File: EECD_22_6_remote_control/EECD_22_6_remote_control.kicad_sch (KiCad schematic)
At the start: 22 parts

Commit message: Add files via upload
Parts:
- gave numbers to parts that had none: 13
- renumbered C to C1
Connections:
- no-connect marks 5 -> 124

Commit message: you can understand at least smth now
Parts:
- C1: value 100u -> 10u
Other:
- note added: "BATTERY"
- note added: "JOYSTICK"
- note added: "LEDs"
- note added: "NRF24"
- moved on the sheet: BT1, BT2, BT3, C1, D1, D2, D3, DC/DC_bck1, R1, R2, R3, R4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

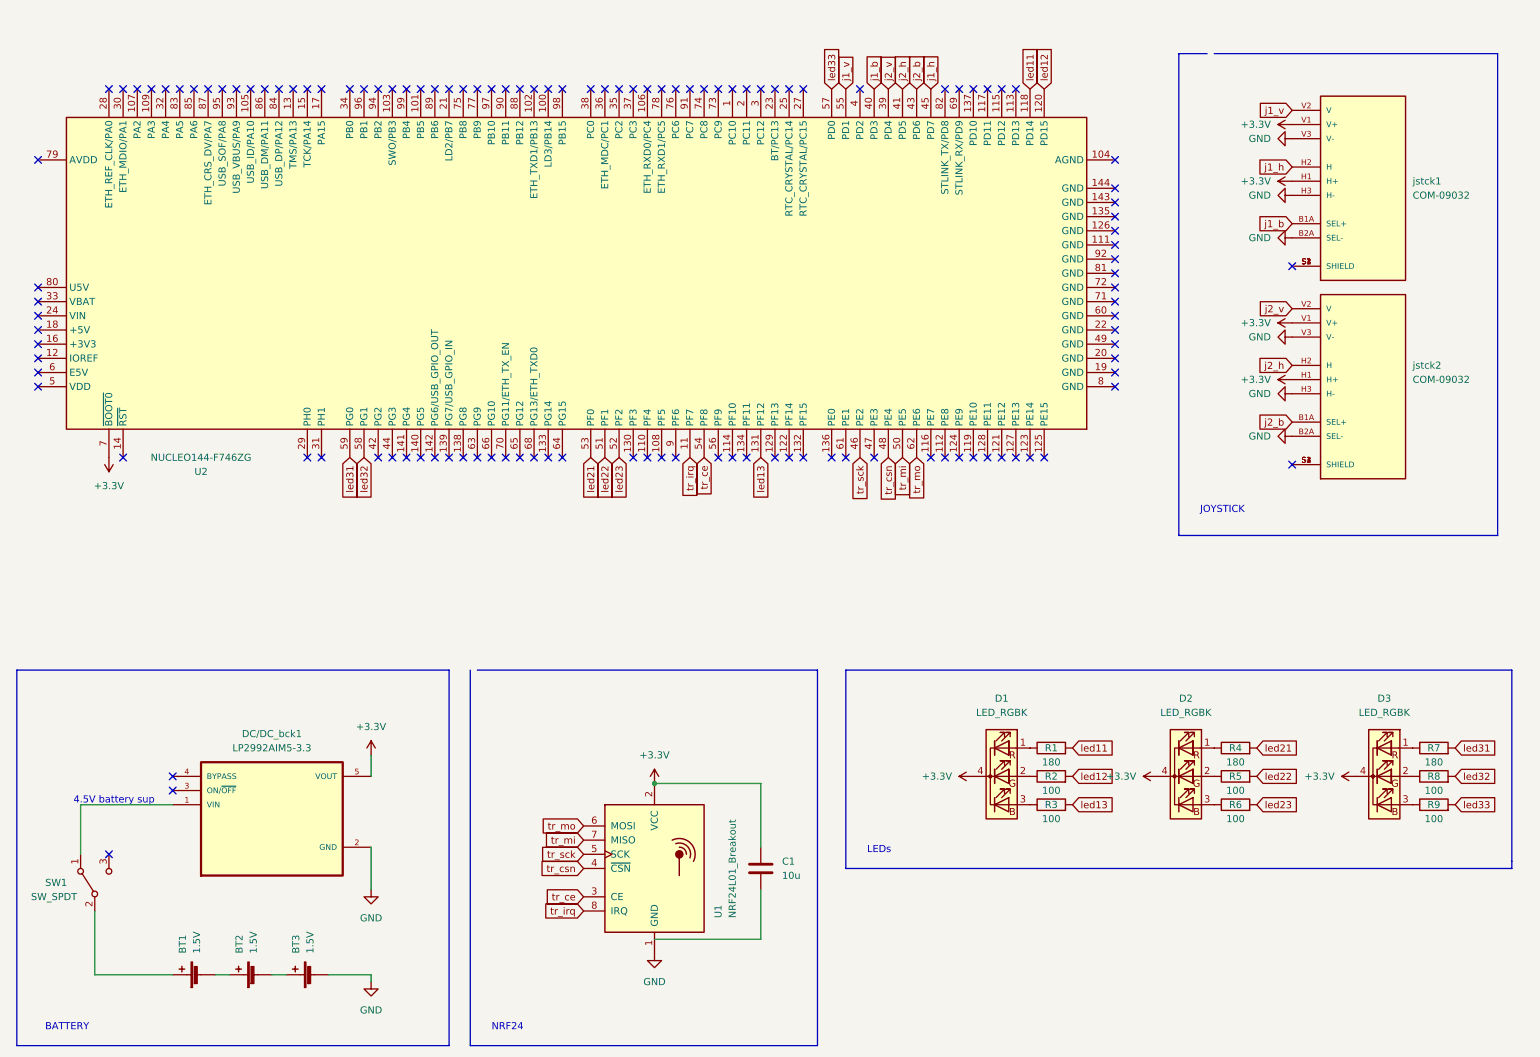
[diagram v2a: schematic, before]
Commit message: normal power supply + footprints
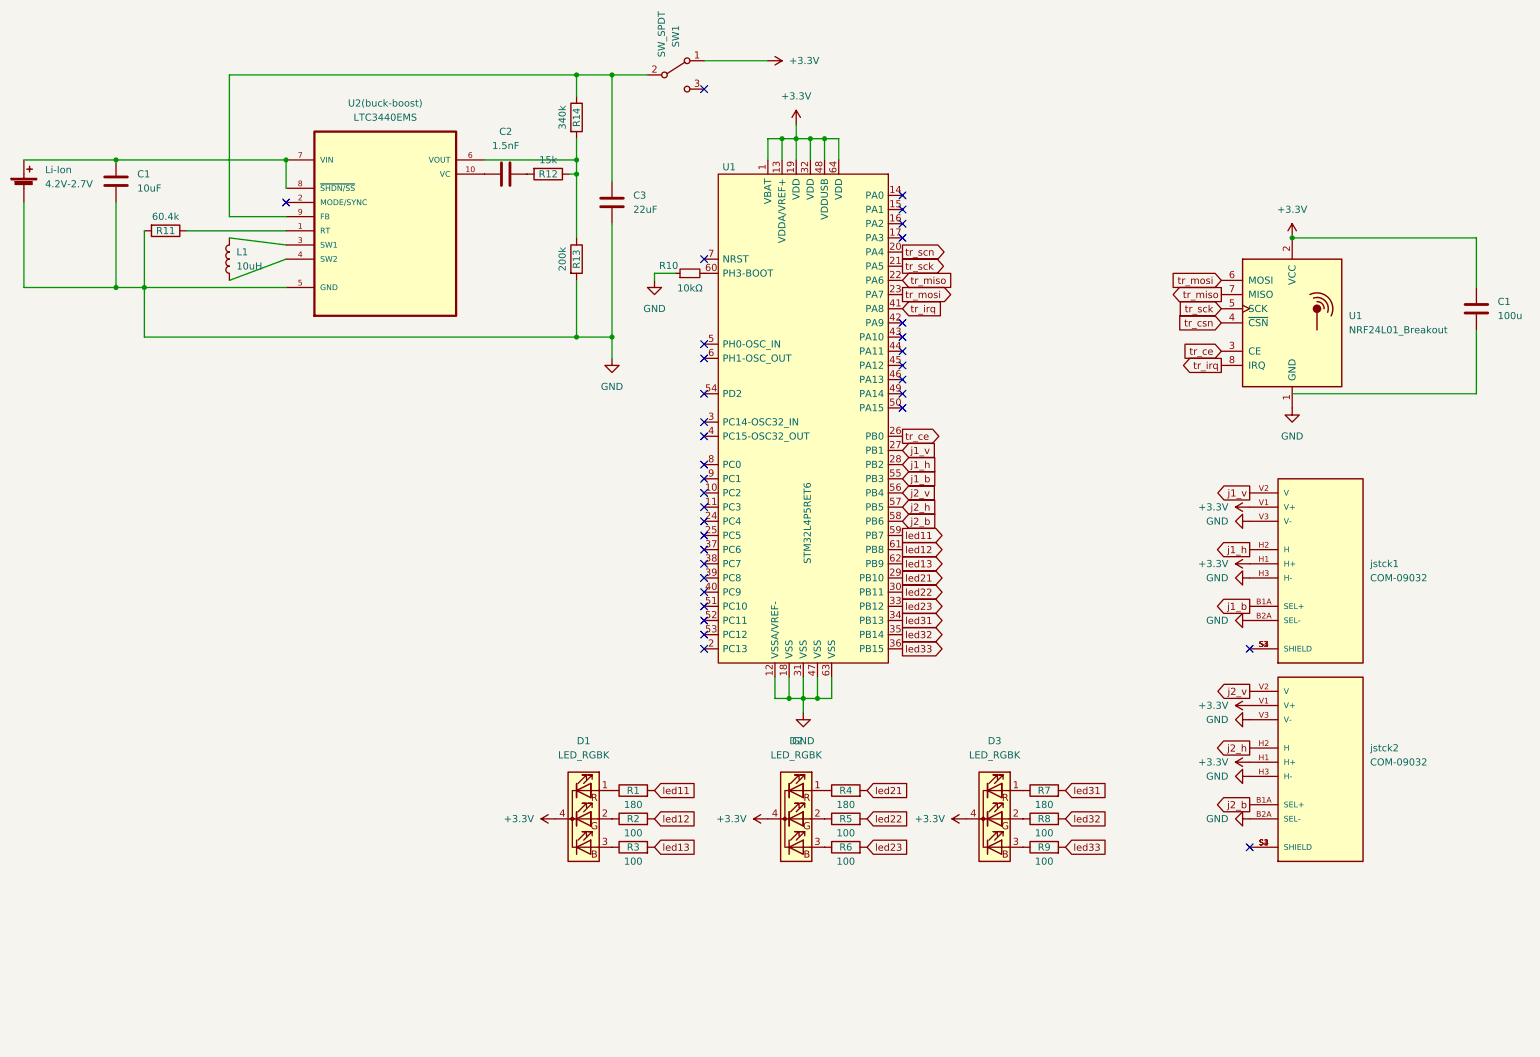
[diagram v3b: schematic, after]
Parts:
- removed BT2, BT3: 1.5V, symbol Device:Battery_Cell
- removed DC/DC_bck1: LP2992AIM5-3.3, SnapEDA Library:SOT95P280X145-5N, symbol LP2992AIM5-3.3:LP2992AIM5-3.3
- removed U2: NUCLEO144-F746ZG, Module:ST_Morpho_Connector_144_STLink, symbol MCU_Module:NUCLEO144-F746ZG
- added C1: 10uF, Capacitor_THT:CP_Axial_L10.0mm_D4.5mm_P15.00mm_Horizontal, symbol Device:C
- added C2: 1.5nF, Capacitor_THT:CP_Axial_L10.0mm_D4.5mm_P15.00mm_Horizontal, symbol Device:C
- added C3: 22uF, Capacitor_THT:CP_Axial_L10.0mm_D4.5mm_P15.00mm_Horizontal, symbol Device:C
- added L1: 10uH, Inductor_SMD:L_6.3x6.3_H3, symbol Device:L
- added R10: 10kΩ, Resistor_SMD:R_0603_1608Metric, symbol Device:R_Small
- added R11: 60.4k, Resistor_SMD:R_0201_0603Metric, symbol Device:R
- added R12: 15k, Resistor_SMD:R_0201_0603Metric, symbol Device:R
- added R13: 200k, Resistor_SMD:R_0201_0603Metric, symbol Device:R
- added R14: 340k, Resistor_SMD:R_0201_0603Metric, symbol Device:R
- added U1: STM32L4P5RET6, Package_QFP:LQFP-64_10x10mm_P0.5mm, symbol Local_Library:STM32L4P5RET6
- added U2(buck-boost): LTC3440EMS, models:SON50P300X300X80-11N-D, symbol LTC3440EMS:LTC3440EMS
- C1: value 10u -> 100u
- Li-Ion: renamed from BT1; value 1.5V -> 4.2V-2.7V
- R1, R2, R3, R4, R5, R6, R7, R8, R9: footprint (none) -> Resistor_SMD:R_0201_0603Metric
- jstck1, jstck2: footprint SnapEDA Library:XDCR_COM-09032 -> models:XDCR_COM-09032
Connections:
- net +3.3V: now also SW1.1 (A), U1.1 (VBAT), U1.13 (VDDA/VREF+), U1.19 (VDD), U1.32 (VDD), U1.48 (VDDUSB), U1.64 (VDD)
- net GND: now also Li-Ion.2 (-), C1.2, C3.1, R10.1, R11.2, R13.2, U1.12 (VSSA/VREF-), U1.18 (VSS), U1.31 (VSS), U1.47 (VSS), U1.63 (VSS), U2(buck-boost).5 (GND)
- net j1_b: now also U1.55 (PB3)
- net j1_h: now also U1.28 (PB2)
- net j1_v: now also U1.27 (PB1)
- net j2_b: now also U1.58 (PB6)
- net j2_h: now also U1.57 (PB5)
- net j2_v: now also U1.56 (PB4)
- net led11: now also U1.59 (PB7)
- net led12: now also U1.61 (PB8)
- net led13: now also U1.62 (PB9)
- net led21: now also U1.29 (PB10)
- net led22: now also U1.30 (PB11)
- net led23: now also U1.33 (PB12)
- net led31: now also U1.34 (PB13)
- net led32: now also U1.35 (PB14)
- net led33: now also U1.36 (PB15)
- net tr_ce: now also U1.26 (PB0)
- net tr_irq: now also U1.41 (PA8)
- net tr_sck: now also U1.21 (PA5)
- net at SW1.2 (B): now also C3.2, R14.1, U2(buck-boost).9 (FB); no longer Li-Ion.1 (+)
- net tr_mi renamed tr_miso
- net tr_miso: now also U1.22 (PA6)
- net tr_mo renamed tr_mosi
- net tr_mosi: now also U1.23 (PA7)
- new net: L1.1, U2(buck-boost).4 (SW2)
- new net: L1.2, U2(buck-boost).3 (SW1)
- new net: R12.1, R13.1, R14.2, U2(buck-boost).6 (VOUT)
- new net: R11.1, U2(buck-boost).1 (RT)
- new net: C2.1, U2(buck-boost).10 (VC)
- new net: C1.1, Li-Ion.1 (+), U2(buck-boost).7 (VIN), U2(buck-boost).8 (~{SHDN/SS})
- new net: R10.2, U1.60 (PH3-BOOT)
- new net: C2.2, R12.2
- new net tr_scn: U1.20 (PA4)
- no-connect marks 124 -> 35
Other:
- note removed: "4.5V battery sup"
- note removed: "BATTERY"
- note removed: "JOYSTICK"
- note removed: "LEDs"
- note removed: "NRF24"
- moved on the sheet: C1, D1, D2, D3, Li-Ion, R1, R2, R3, R4, R5, R6, R7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
